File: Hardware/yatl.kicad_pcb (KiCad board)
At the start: 4 copper layers, 56.6 x 25.4 mm, 19 parts, among them J1 Conn_01x08_Male, J2 Conn_01x08_Male, SW1 SW_SPST, U2 ATmega328-A

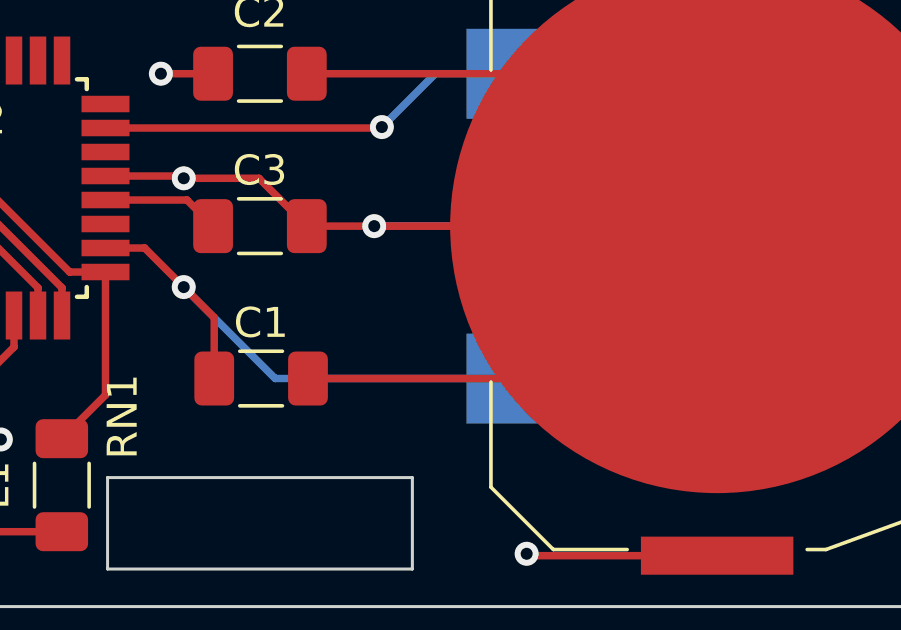
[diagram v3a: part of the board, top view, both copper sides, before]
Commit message: Remove LMT86 decoupling capacitor that cause sudden temperature spike after certain minutes
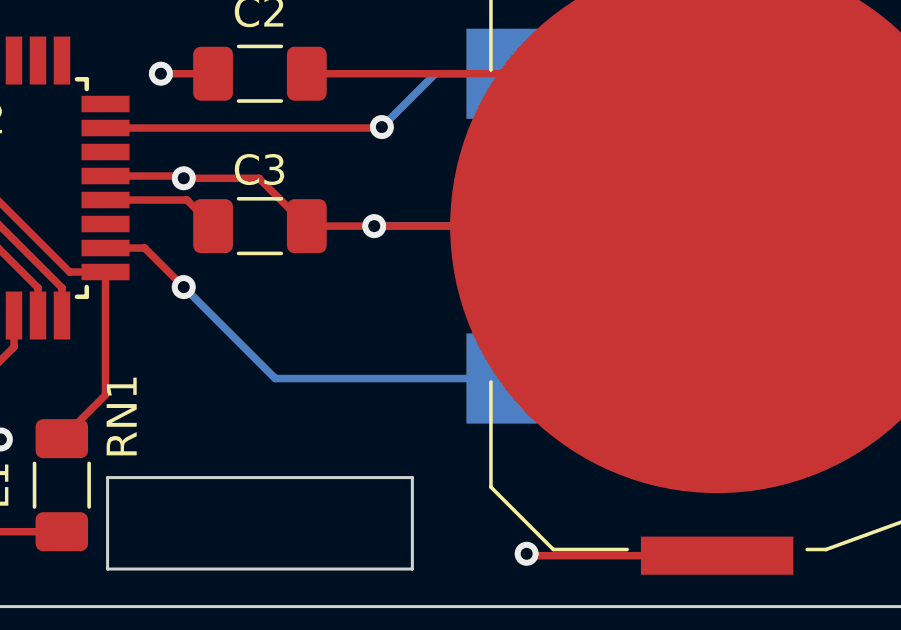
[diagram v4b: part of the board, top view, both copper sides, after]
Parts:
- removed C1: 100n, Capacitor_SMD:C_1206_3216Metric_Pad1.33x1.80mm_HandSolder
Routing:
- net GND: track 94.3 -> 78.5 mm
- net VCC: track 45.8 -> 42.4 mm
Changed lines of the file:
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@@
-    )
-  )
-  (footprint "Capacitor_SMD:C_1206_3216Metric_Pad1.33x1.80mm_HandSolder" (layer "F.Cu")
-    (at 201.4605 109.22)
-    (descr "Capacitor SMD 1206 (3216 Metric), square (rectangular) end terminal, IPC_7351 nominal with elongated pad for handsoldering. (Body size source: IPC-SM-782 page 76, https://www.pcb-3d.com/wordpress/wp-content/uploads/ipc-sm-782a_amendment_1_and_2.pdf), generated with kicad-footprint-generator")
-    (tags "capacitor handsolder")
-    (property "Sheetfile" "yatl.kicad_sch")
-    (property "Sheetname" "")
-    (attr smd)
-    (fp_text reference "C1" (at 0 -1.85) (layer "F.SilkS")
-      (effects (font (size 1 1) (thickness 0.15)))
-    )
-    (fp_text value "100n" (at 0 1.85) (layer "F.Fab")
-      (effects (font (size 1 1) (thickness 0.15)))
-    )
-    (fp_text user "${REFERENCE}" (at 0 0) (layer "F.Fab")
-      (effects (font (size 0.8 0.8) (thickness 0.12)))
-    )
-    (fp_line (start -0.711252 0.91) (end 0.711252 0.91) (layer "F.SilkS") (width 0.12))
-    (fp_line (start -0.711252 -0.91) (end 0.711252 -0.91) (layer "F.SilkS") (width 0.12))
-    (fp_line (start 2.48 -1.15) (end 2.48 1.15) (layer "F.CrtYd") (width 0.05))
-    (fp_line (start -2.48 -1.15) (end 2.48 -1.15) (layer "F.CrtYd") (width 0.05))
-    (fp_line (start 2.48 1.15) (end -2.48 1.15) (layer "F.CrtYd") (width 0.05))
-    (fp_line (start -2.48 1.15) (end -2.48 -1.15) (layer "F.CrtYd") (width 0.05))
-    (fp_line (start -1.6 -0.8) (end 1.6 -0.8) (layer "F.Fab") (width 0.1))
-    (fp_line (start 1.6 0.8) (end -1.6 0.8) (layer "F.Fab") (width 0.1))
-    (fp_line (start 1.6 -0.8) (end 1.6 0.8) (layer "F.Fab") (width 0.1))
-    (fp_line (start -1.6 0.8) (end -1.6 -0.8) (layer "F.Fab") (width 0.1))
-    (pad "1" smd roundrect (at -1.5625 0) (size 1.325 1.8) (layers "F.Cu" "F.Paste" "F.Mask") (roundrect_rratio 0.1886792453)
-      (net 1 "VCC") (pintype "passive"))
-    (pad "2" smd roundrect (at 1.5625 0) (size 1.325 1.8) (layers "F.Cu" "F.Paste" "F.Mask") (roundrect_rratio 0.1886792453)
-      (net 2 "GND") (pintype "passive"))
-    (model "${KICAD6_3DMODEL_DIR}/Capacitor_SMD.3dshapes/C_1206_3216Metric.wrl"
-      (offset (xyz 0 0 0))
-      (scale (xyz 1 1 1))
-      (rotate (xyz 0 0 0))
     )
   )
@@
   (segment (start 208.089 93.155) (end 208.026 93.218) (width 0.25) (layer "F.Cu") (net 1))
   (segment (start 210.375 115.125) (end 210.312 115.062) (width 0.25) (layer "F.Cu") (net 1))
-  (segment (start 199.898 107.188) (end 198.882 106.172) (width 0.25) (layer "F.Cu") (net 1))
   (segment (start 199.8595 99.06) (end 198.12 99.06) (width 0.25) (layer "F.Cu") (net 1))
   (segment (start 187.774 104.07) (end 185.49 104.07) (width 0.25) (layer "F.Cu") (net 1))
   (segment (start 216.662 93.155) (end 208.089 93.155) (width 0.25) (layer "F.Cu") (net 1))
   (segment (start 185.42 104.14) (end 185.42 104.194003) (width 0.25) (layer "F.Cu") (net 1))
-  (segment (start 199.898 109.22) (end 199.898 107.188) (width 0.25) (layer "F.Cu") (net 1))
   (segment (start 187.774 102.47) (end 184.296 102.47) (width 0.25) (layer "F.Cu") (net 1))
   (segment (start 185.49 104.07) (end 185.42 104.14) (width 0.25) (layer "F.Cu") (net 1))
@@
   (segment (start 176.365 98.895) (end 178.852 98.895) (width 0.25) (layer "F.Cu") (net 2))
   (segment (start 187.774 103.27) (end 185.4955 103.27) (width 0.25) (layer "F.Cu") (net 2))
-  (segment (start 203.023 109.22) (end 211.582 109.22) (width 0.25) (layer "F.Cu") (net 2))
   (segment (start 196.274 102.47) (end 198.8065 102.47) (width 0.25) (layer "F.Cu") (net 2))
-  (segment (start 211.582 109.22) (end 216.662 104.14) (width 0.25) (layer "F.Cu") (net 2))
   (segment (start 173.99 102.435) (end 176.276 104.721) (width 0.25) (layer "F.Cu") (net 2))
   (segment (start 202.9845 99.06) (end 211.582 99.06) (width 0.25) (layer "F.Cu") (net 2))
